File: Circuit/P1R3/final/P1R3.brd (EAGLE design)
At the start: 59.7 x 59.7 mm, 88 parts, among them J1 MICRO_USB_B_HIROSE_ZX62R-B-5P, U1 MK20DX256VLH7, U2 TPS61200, U3 MPU-9250, Y1 32.768KHz, Y2 16Mhz/8pF, Y3 26 Mhz, Y4 16 Mhz

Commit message: Added four from LED drivers to R4. Corrected R3 bootloader circuit. Rerouted switch in schematic and board on both R3 and R4 for proper isolation of USB and lipo voltage. Ready for final review
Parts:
- added C39: 0.1uF, appfruits:0603-CAP
- added L9: 2.2uH, 2.1A, appfruits:LPS3015
- moved S2 1.50 mm to (27.8, 57.3)
- moved LED4 0.05 mm to (50.9, 29.7)
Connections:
- removed net VRAW: JP5.2, S1.2
- new net N$40: L9.2
- new net VBAT: JP5.2, S1.3
- new net VUSB: J1.1, S1.1
- net GND: now also C39.2, L9.1
- net N$49: now also C39.1
- net VCC: now also S1.2; no longer J1.1, S1.1
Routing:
- net VUSB: track 0.00 -> 62.1 mm, vias 0 -> 2
- net VCC: track 74.9 -> 37.3 mm, vias 4 -> 2
- net VBAT: track 0.00 -> 14.8 mm
- net VRAW: track 12.7 -> 0.00 mm
- net N$42: track 0.00 -> 10.7 mm
- net N$41: track 0.00 -> 10.5 mm
- net N$49: track 0.00 -> 2.88 mm
- net N$75: track 15.4 -> 16.8 mm
- net GND: track 40.9 -> 40.0 mm, vias 125 -> 128
- net 3.3V: track 339.4 -> 338.9 mm

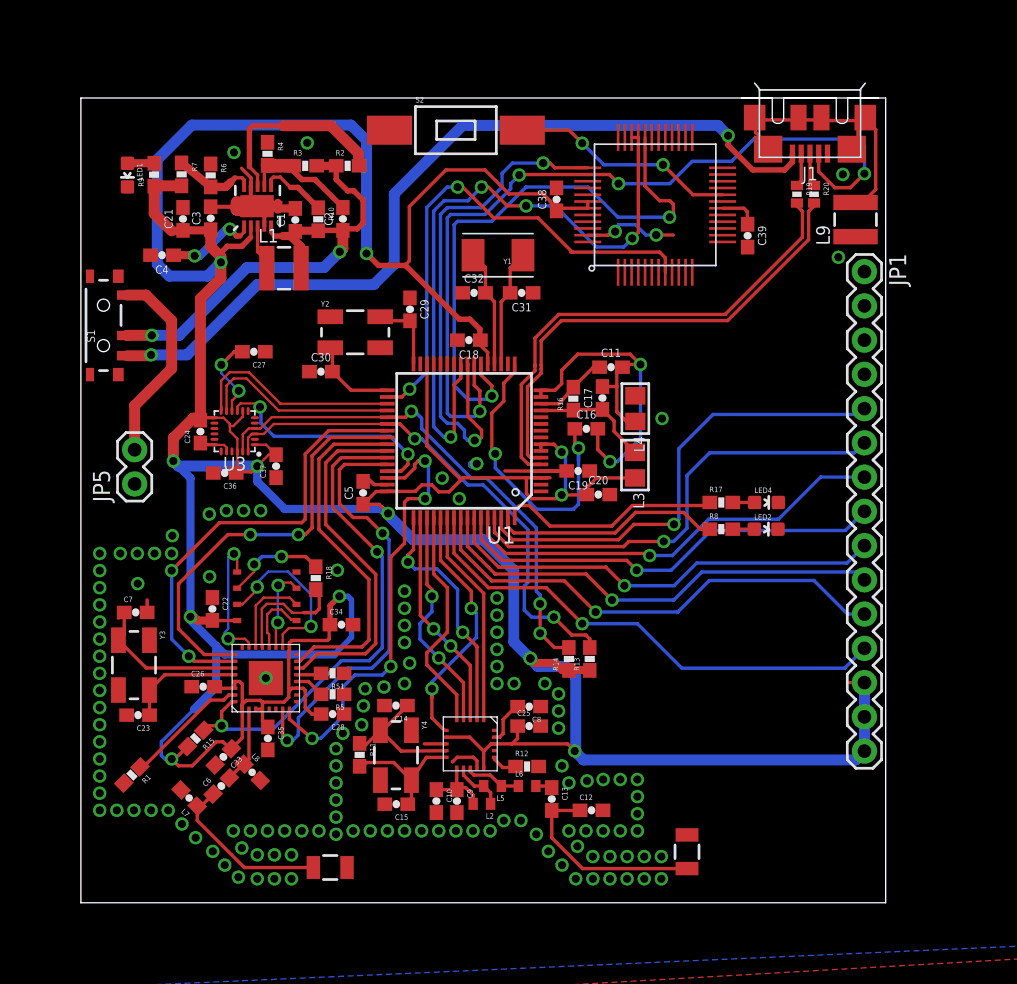
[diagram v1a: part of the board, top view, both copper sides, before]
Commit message: R3 and R4 DRC checked and ready for final review
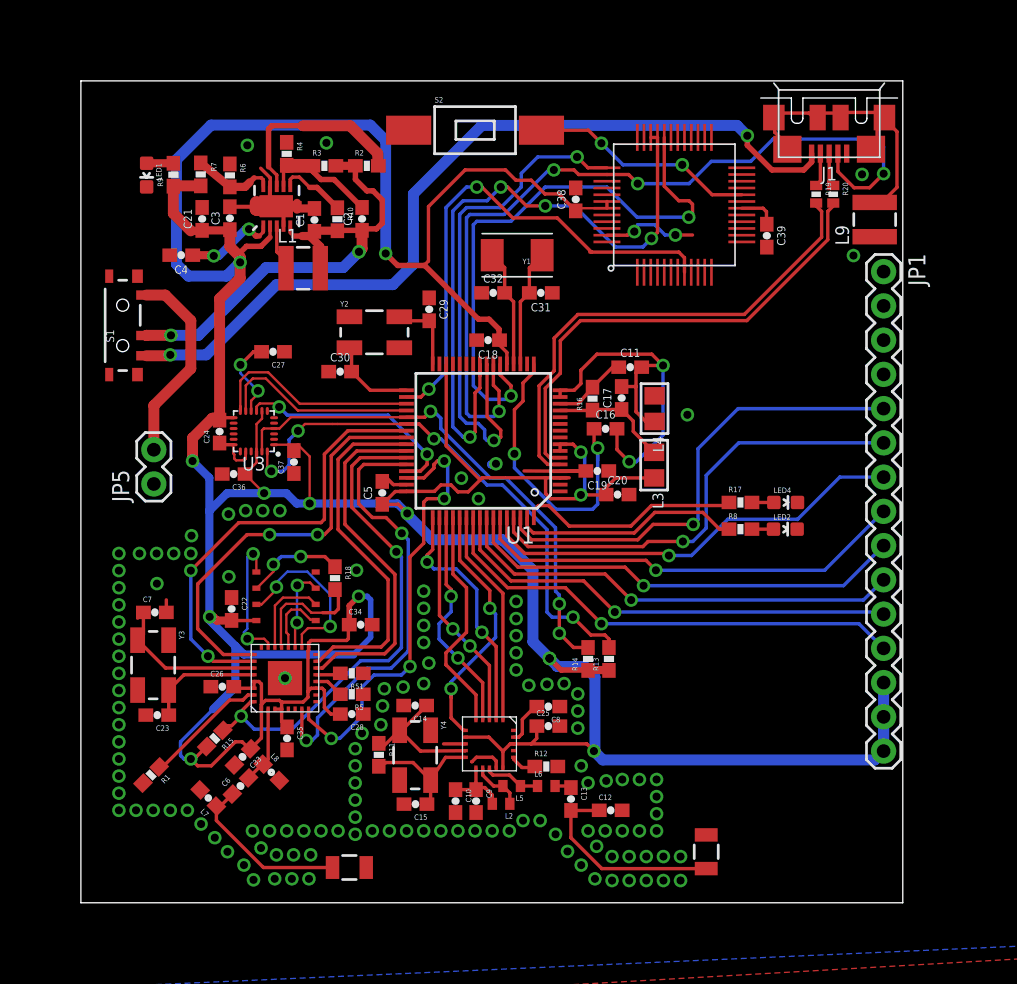
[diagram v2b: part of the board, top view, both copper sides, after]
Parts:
- moved C13 1.42 mm to (36.3, 7.70)
- moved C14 1.42 mm to (24.8, 14.6)
- moved C17 1.42 mm to (40.1, 37.4)
- moved C18 1.42 mm to (30.2, 41.7)
- moved C20 1.42 mm to (39.8, 30.3)
- moved C31 1.42 mm to (34.1, 45.2)
- moved C32 1.42 mm to (30.6, 45.2)
- moved C38 1.42 mm to (36.7, 52.2)
- moved J1 1.42 mm to (55.5, 59.7)
- moved L4 1.42 mm to (42.5, 36.7)
- moved L9 1.42 mm to (58.9, 50.7)
- moved LED4 1.42 mm to (52.3, 29.7)
- moved R13 1.42 mm to (39.2, 18.1)
- moved R14 1.42 mm to (37.6, 18.1)
- moved R16 1.42 mm to (37.9, 37.4)
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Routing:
- net N$45: track 0.00 -> 4.27 mm
- net 3.3V: track 338.9 -> 336.2 mm, vias 13 -> 14
- net SDA: track 38.5 -> 40.7 mm, vias 2 -> 4
- net GND: track 40.0 -> 42.0 mm
- net PTC11: track 36.2 -> 34.3 mm
- net N$42: track 10.7 -> 9.08 mm
- net PTC10: track 37.2 -> 36.0 mm
- net AD0: track 17.8 -> 17.1 mm
- net VREFL: track 28.8 -> 29.4 mm
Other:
- board size 59.7 x 59.7 mm -> 61 x 61 mm

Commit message: R3 and R4 shippable. Ordering PCBs
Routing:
- net GND: vias 128 -> 144
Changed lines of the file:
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@@
 <setting verticaltext="up"/>
 </settings>
-<grid distance="5" unitdist="mil" unit="mil" style="lines" multiple="1" display="yes" altdistance="0.025" altunitdist="inch" altunit="inch"/>
+<grid distance="1" unitdist="mil" unit="mil" style="lines" multiple="1" display="yes" altdistance="0.025" altunitdist="inch" altunit="inch"/>
 <layers>
 <layer number="1" name="Top" color="4" fill="1" visible="yes" active="yes"/>
@@
 <wire x1="11.303" y1="33.3248" x2="11.303" y2="33.9518" width="0.1778" layer="1"/>
 <wire x1="11.303" y1="33.9518" x2="11.327" y2="33.9758" width="0.1778" layer="1"/>
+<via x="42.5704" y="15.5702" extent="1-16" drill="0.6"/>
+<via x="48.8696" y="15.5194" extent="1-16" drill="0.6"/>
+<via x="54.737" y="15.621" extent="1-16" drill="0.6"/>
+<via x="52.6796" y="8.0518" extent="1-16" drill="0.6"/>
+<via x="46.2026" y="7.9756" extent="1-16" drill="0.6"/>
+<via x="17.5768" y="7.874" extent="1-16" drill="0.6"/>
+<via x="5.969" y="2.9464" extent="1-16" drill="0.6"/>
+<via x="2.5654" y="28.7274" extent="1-16" drill="0.6"/>
+<via x="2.413" y="35.941" extent="1-16" drill="0.6"/>
+<via x="2.9718" y="49.5808" extent="1-16" drill="0.6"/>
+<via x="3.0226" y="54.1528" extent="1-16" drill="0.6"/>
+<via x="2.8956" y="58.2676" extent="1-16" drill="0.6"/>
+<via x="16.002" y="43.2308" extent="1-16" drill="0.6"/>
+<via x="37.4904" y="46.5582" extent="1-16" drill="0.6"/>
+<via x="48.4886" y="39.3954" extent="1-16" drill="0.6"/>
+<via x="55.0164" y="41.783" extent="1-16" drill="0.6"/>
+<wire x1="59.5376" y1="41.7322" x2="55.0164" y2="41.783" width="0" layer="19" extent="1-1"/>
 </signal>
 <signal name="N$2">
